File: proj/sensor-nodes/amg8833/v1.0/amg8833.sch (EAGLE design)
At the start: 54 parts, among them J1 54602-908LF, J2 54602-908LF, U1 AMG8833, U2 PCA9615DPJ, U3 MIC4680YM-TR, U4 LM2937IMP3.3NOPB

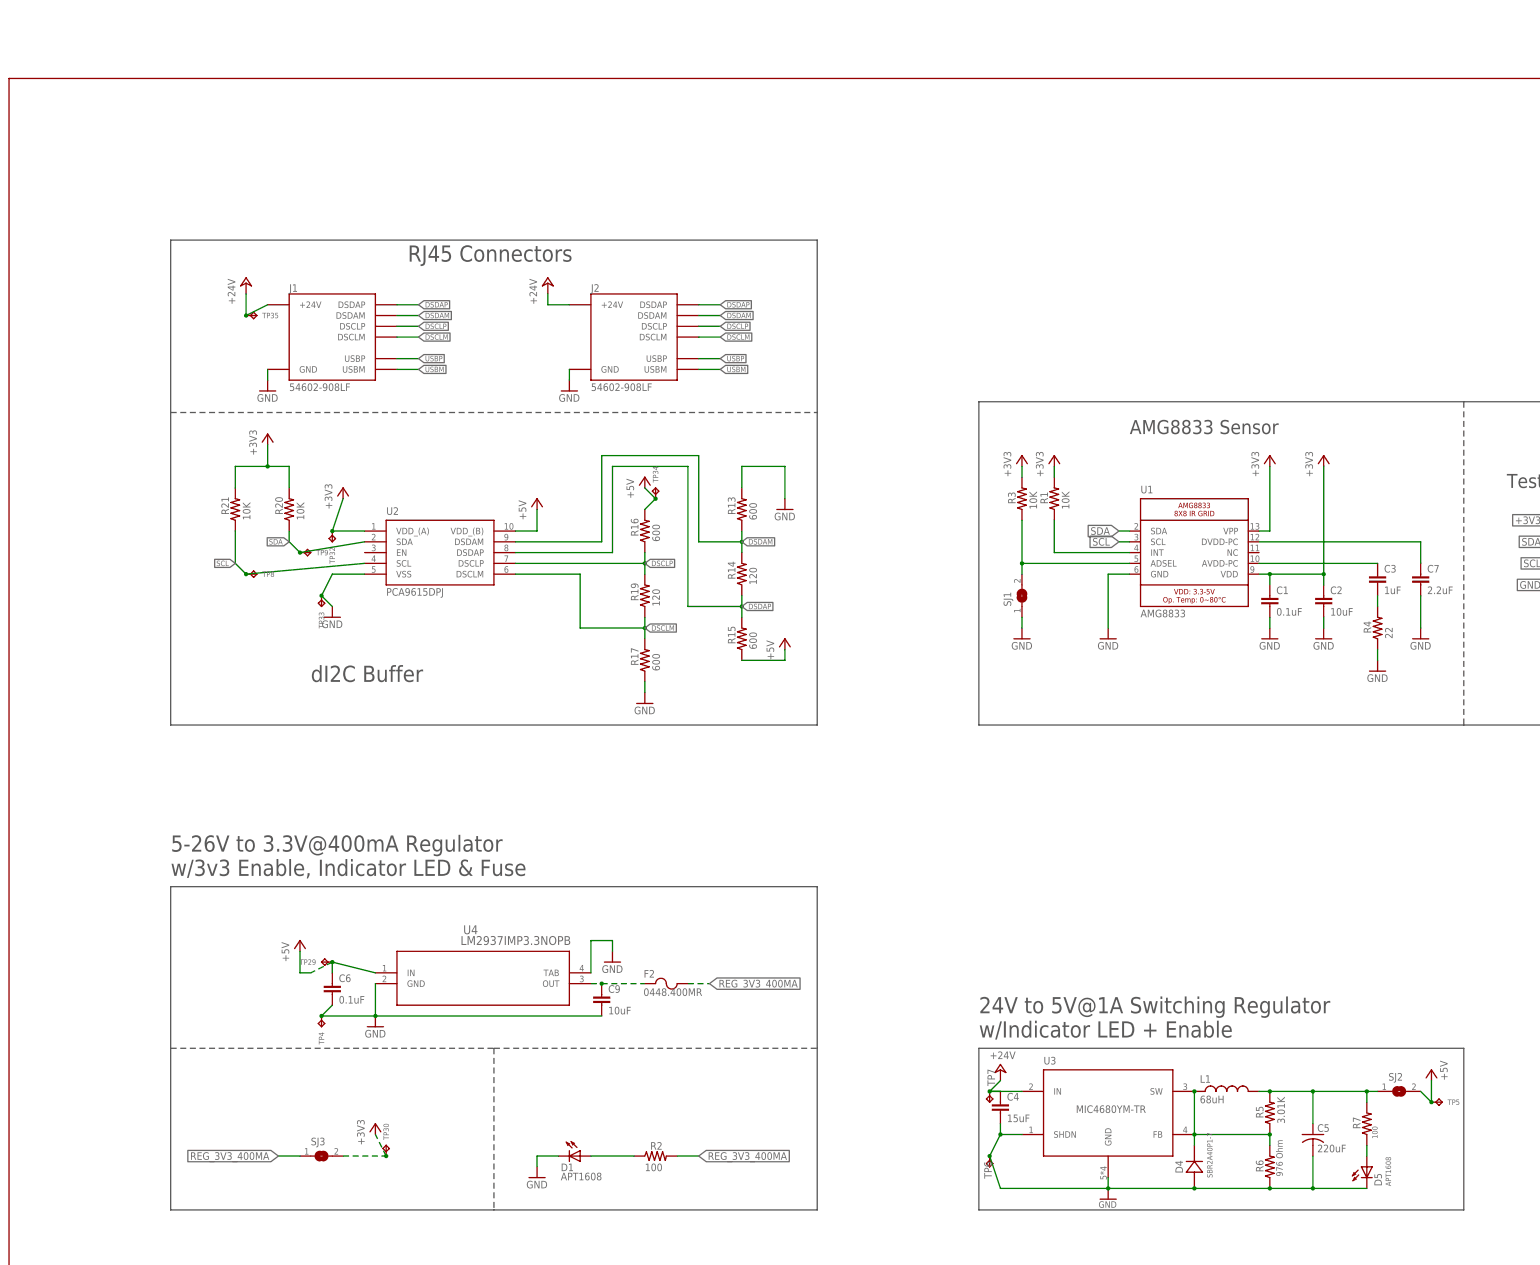
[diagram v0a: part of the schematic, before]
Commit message: added atlas sensor port design block
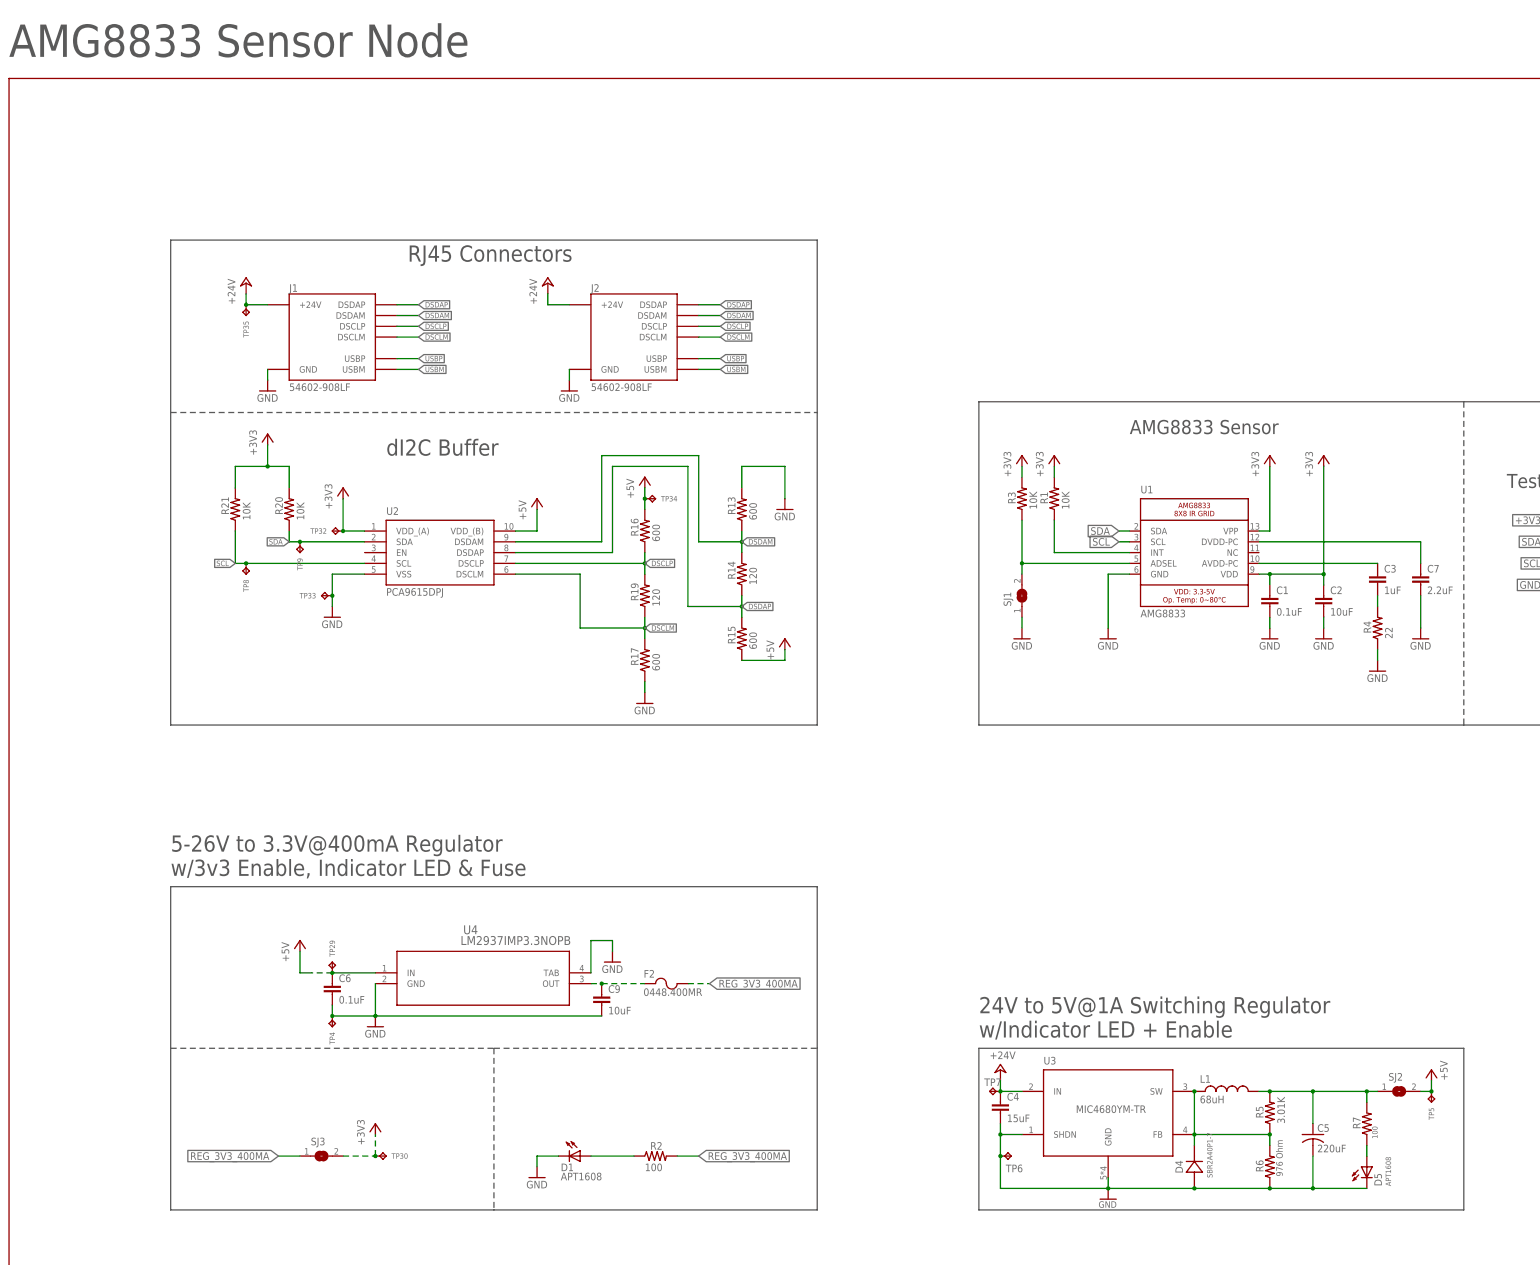
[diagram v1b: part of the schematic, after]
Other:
- note added: "AMG8833 Sensor Node"
- moved on the sheet: TP29, TP30, TP32, TP33, TP34, TP35, TP4, TP5, TP6, TP7, TP8, TP9
